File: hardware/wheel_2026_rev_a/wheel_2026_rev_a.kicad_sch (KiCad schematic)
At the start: 19 parts, among them J1 OTHER, J2 RPI, U1 LM358, U2 TCRT5000, U3 MLX90614

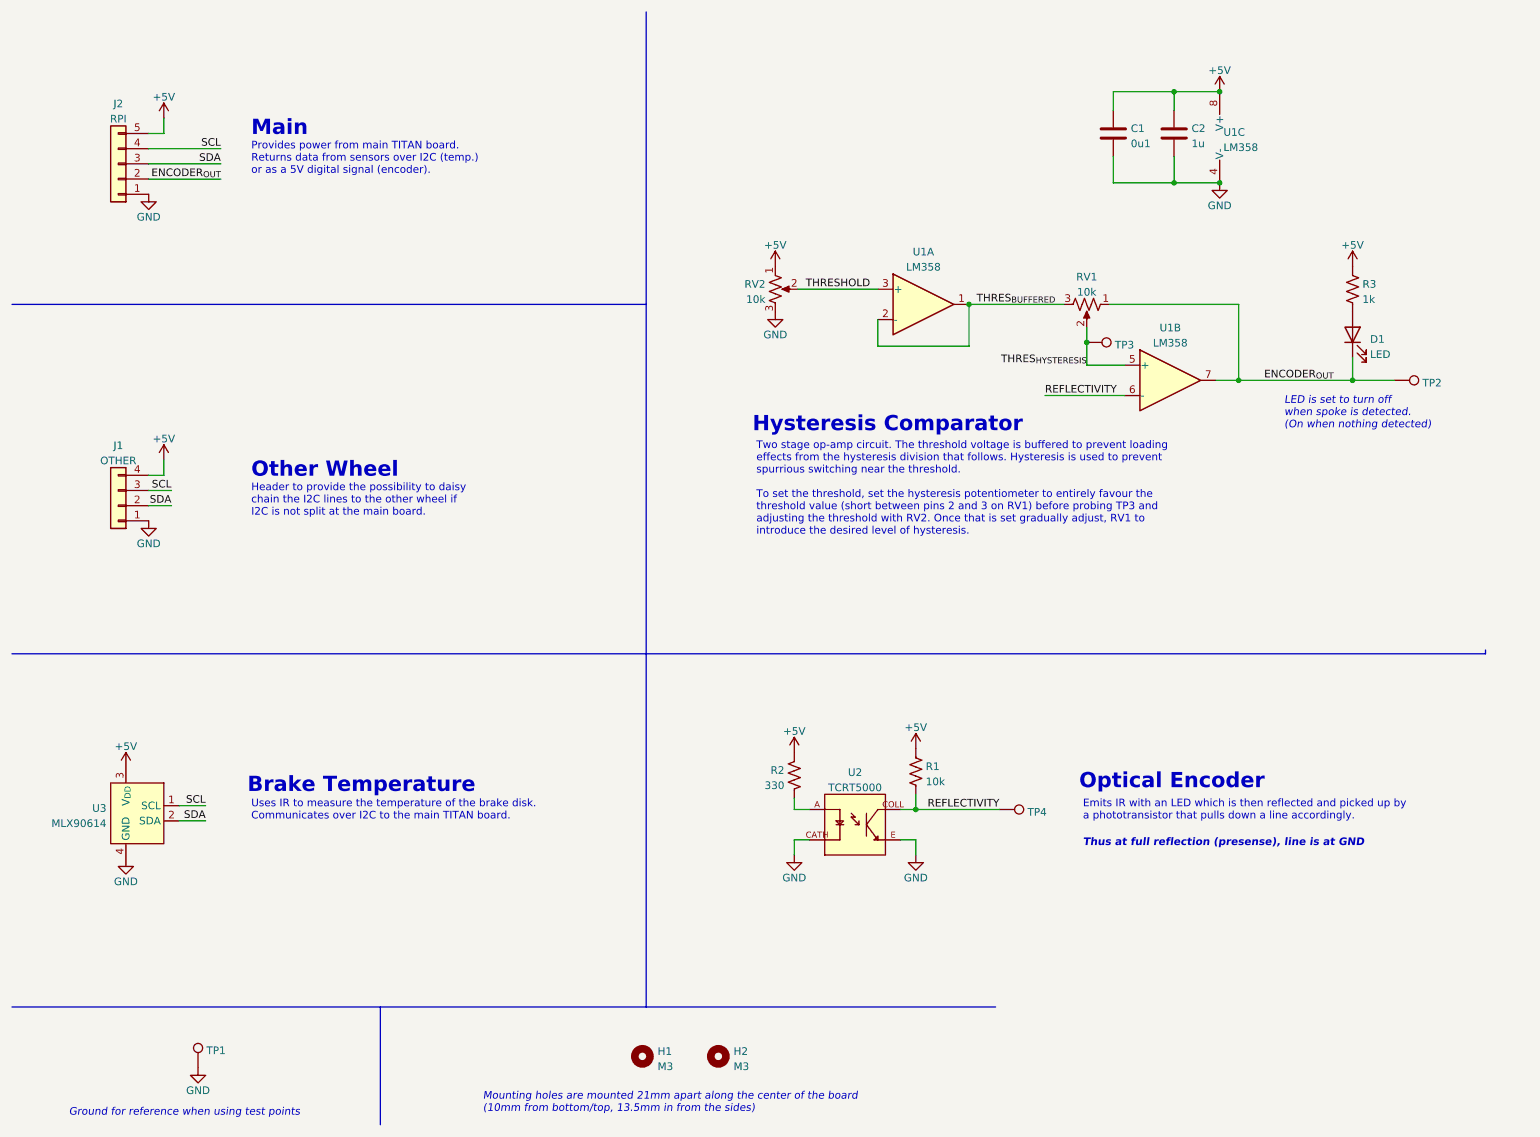
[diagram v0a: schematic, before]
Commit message: Brought KiCad projects into KiCad 10.0
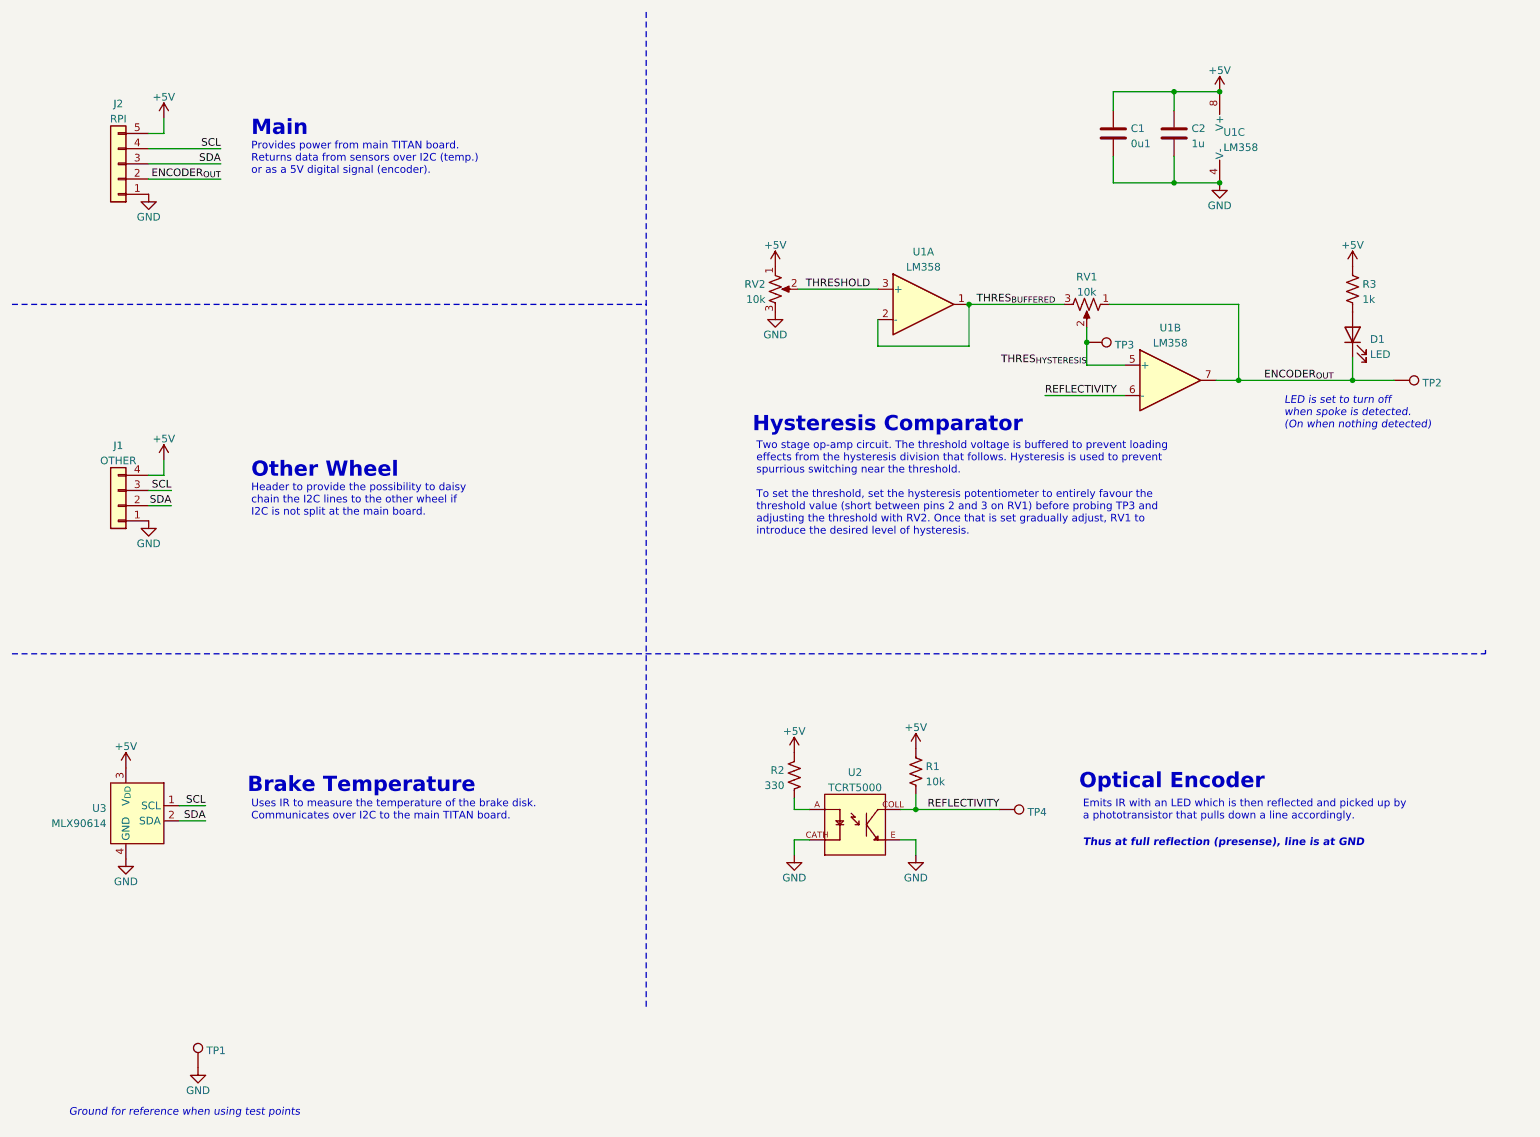
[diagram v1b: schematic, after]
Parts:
- removed H1, H2: M3, MountingHole:MountingHole_3.2mm_M3, symbol Mechanical:MountingHole
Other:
- note removed: "Mounting holes are mounted 21mm apart along the center of the board (10mm from bottom/top, 13.5mm in from the sides)"

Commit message: Revised wheel sensor board and documentation
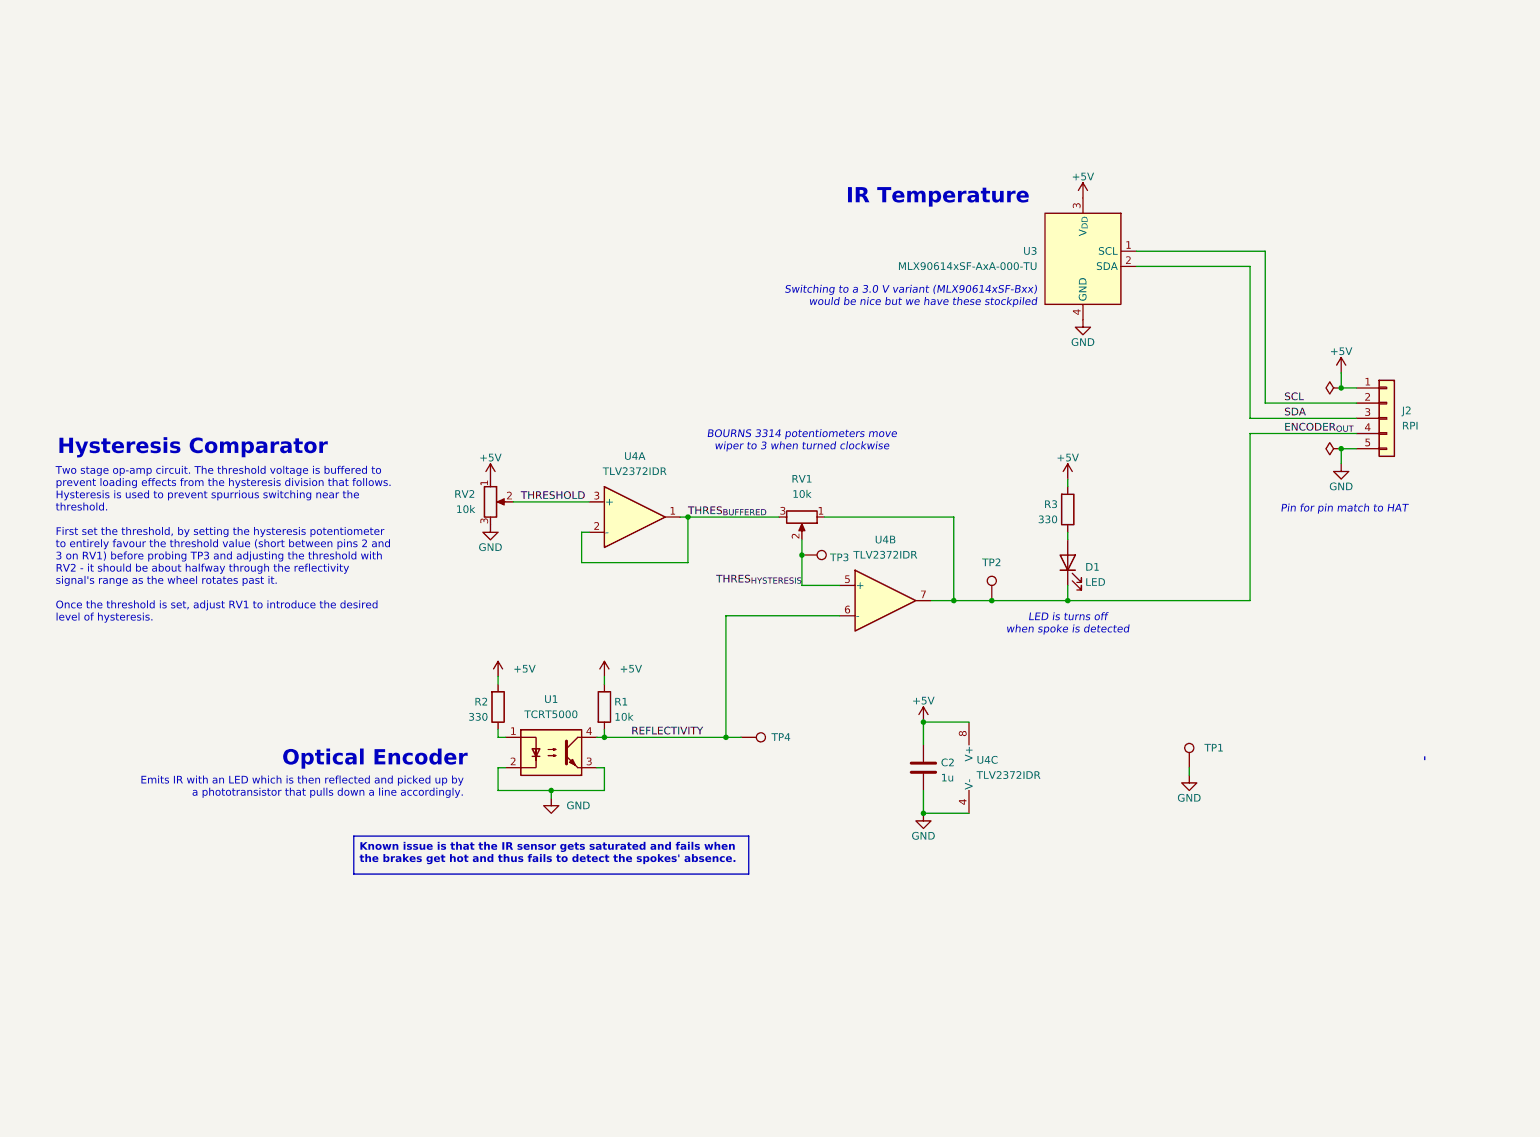
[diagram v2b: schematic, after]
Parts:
- removed C1: 0u1, Capacitor_SMD:C_0603_1608Metric, symbol Device:C
- removed J1: OTHER, Connector_PinHeader_2.54mm:PinHeader_1x04_P2.54mm_Vertical, symbol Connector_Generic:Conn_01x04
- removed R3: 1k, Resistor_SMD:R_0603_1608Metric, symbol Device:R_US
- removed U1: LM358, Package_SO:SOIC-8_3.9x4.9mm_P1.27mm, symbol Amplifier_Operational:LM358
- removed U2: TCRT5000, TCRT5000:OPTO_TCRT5000, symbol TCRT5000:TCRT5000
- added R3: 330, Resistor_SMD:R_0603_1608Metric, symbol Device:R
- added U1: TCRT5000, TITAN:OPTO_TCRT5000, symbol Isolator:Optocoupler_DC_PhotoNPN_AKEC
- added U4: TLV2372IDR, Package_SO:SOIC-8_3.9x4.9mm_P1.27mm, symbol Amplifier_Operational:TLV2372
- C2: LCSC (none) -> C15849
- D1: LCSC (none) -> C2297
- J2: footprint Connector_PinHeader_2.54mm:PinHeader_1x05_P2.54mm_Vertical -> TITAN:WirePads_1x05_P2.54mm; LCSC (none) -> N/A
- R1: symbol Device:R_US -> Device:R; LCSC (none) -> C25804
- R2: symbol Device:R_US -> Device:R; LCSC (none) -> C23138
- RV1, RV2: footprint Potentiometer_THT:Potentiometer_Vishay_T73YP_Vertical -> Potentiometer_SMD:Potentiometer_Bourns_3314J_Vertical; symbol Device:R_Potentiometer_US -> Device:R_Potentiometer; LCSC (none) -> C36376
- TP1, TP2, TP3, TP4: footprint TestPoint:TestPoint_Bridge_Pitch2.54mm_Drill1.0mm -> TestPoint:TestPoint_Pad_D3.0mm; LCSC (none) -> N/A
- U3: value MLX90614 -> MLX90614xSF-AxA-000-TU; symbol wheel_sensors:MLX90614 -> TITAN:MLX90614; MANUFACTURER (none) -> Melexis
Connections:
- net +5V: now also J2.1 (Pin_1), R3.2, U4.8 (V+); no longer J2.5 (Pin_5)
- net ENCODER_{OUT}: now also J2.4 (Pin_4), U4.7; no longer J2.2 (Pin_2)
- net GND: now also J2.5 (Pin_5), U1.2, U1.3, U4.4 (V-); no longer J2.1 (Pin_1)
- net REFLECTIVITY: now also U1.4, U4.6 (-)
- net SCL: now also J2.2 (Pin_2); no longer J2.4 (Pin_4)
- net THRESHOLD: now also U4.3 (+)
- net THRES_{BUFFERED}: now also U4.1, U4.2 (-)
- net THRES_{HYSTERESIS}: now also U4.5 (+)
- net at R2.1: now also U1.1
- net at D1.2 (A): now also R3.1
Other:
- note added: "BOURNS 3314 potentiometers move wiper to 3 when turned clockwise"
- note added: "IR Temperature"
- note added: "LED is turns off when spoke is detected"
- note added: "Pin for pin match to HAT"
- note added: "Switching to a 3.0 V variant (MLX90614xSF-Bxx) would be nice but we have these stockpiled"
- note removed: "Brake Temperature"
- note removed: "Ground for reference when using test points"
- note removed: "Header to provide the possibility to daisy chain the I2C lines to the other wheel if I2C is not split at the main board."
- note removed: "LED is set to turn off when spoke is detected. (On when nothing detected)"
- note removed: "Main"
- note removed: "Other Wheel"
- note removed: "Provides power from main TITAN board. Returns data from sensors over I2C (temp.) or as a 5V digital signal (encoder)."
- note removed: "Thus at full reflection (presense), line is at GND"
- note removed: "Two stage op-amp circuit. The threshold voltage is buffered to prevent loading effects from the hysteresis division that follows. Hysteresis is used to prevent spurrious switching near the threshold. To set the threshold, set the hysteresis potentiometer to entirely favour the threshold value (short between pins 2 and 3 on RV1) before probing TP3 and adjusting the threshold with RV2. Once that is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"
- note removed: "Uses IR to measure the temperature of the brake disk. Communicates over I2C to the main TITAN board."
- company: HPVDT -> Savo Bajic
- title: TITAN Wheel Sensor Board -> TITAN 2026 Wheel Sensor
- moved on the sheet: C2, D1, J2, TP1, TP3, TP4, U3
